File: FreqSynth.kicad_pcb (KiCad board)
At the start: 4 copper layers, 79 x 50 mm, 135 parts, among them IC1 ATMEGA32U2, P1 CPL-CON-BARREL-2.1MM, P2 RF1, P3 RF2P, P4 RF2N, P5 USB_MINI_B, P6 CONN_01X03, P7 REF_IN, P8 RESET, U1 MAX2870, U10 PE43711, U11 LMH2110, U2 TS5A3159, U3 TLV7113333DDSET, U4 AP65101, U5 TLV7113333DDSET, U6 RT9069-50GB, U7 SKY13322-375LF, U8 SKY13322-375LF, U9 TRF37A75, X1 25MHz ±5ppm 3.3V 33mA, X2 8MHz 18PF 50ppm

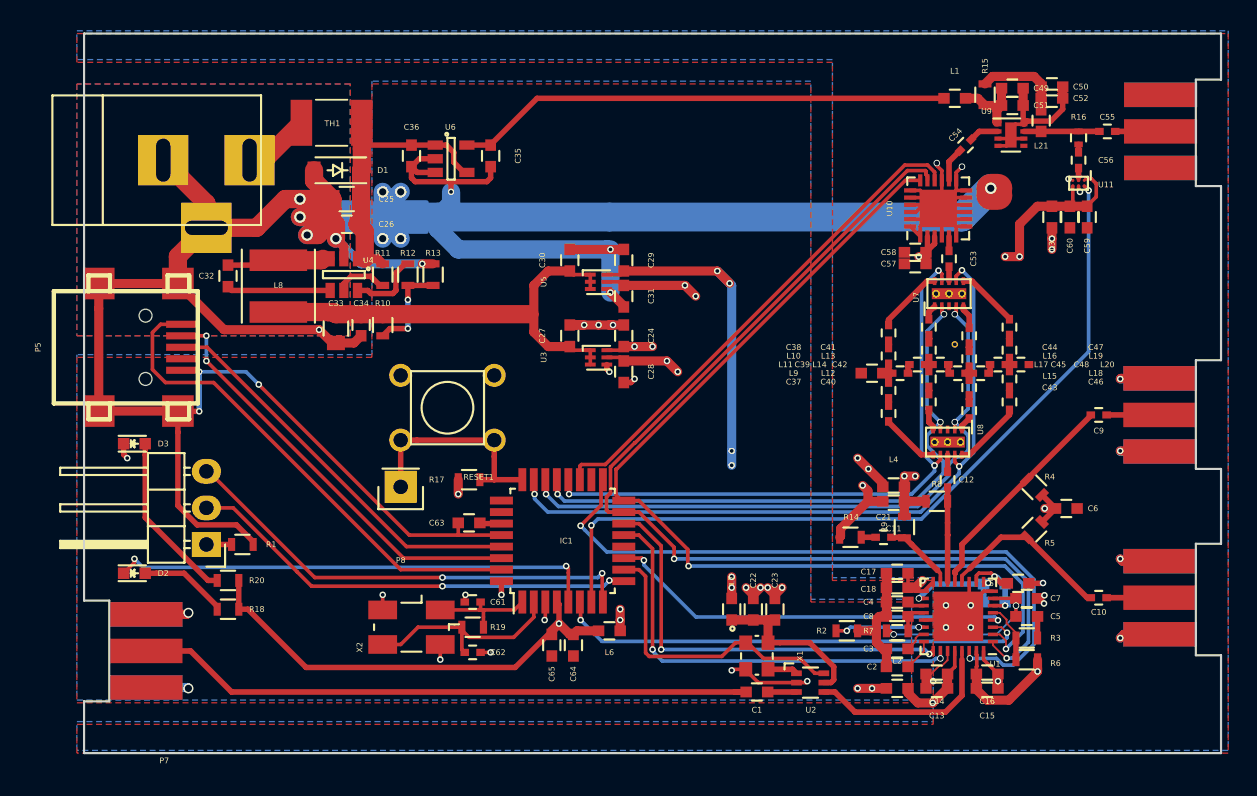
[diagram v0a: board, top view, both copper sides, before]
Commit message: Board layout done, no ERC or DRC:s left
Signed-off-by: Martin Berglund <LeastSignificantBit@users.noreply.github.com>
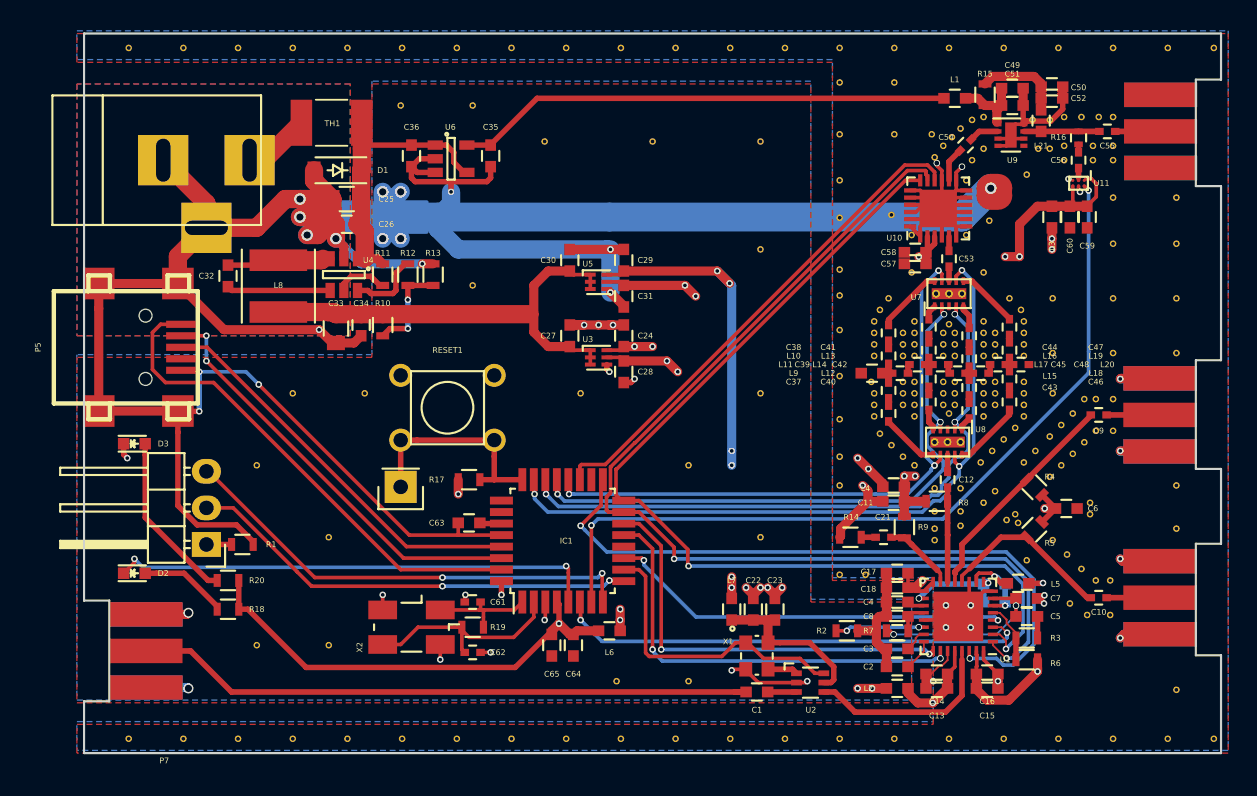
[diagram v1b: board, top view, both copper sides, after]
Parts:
- added ?: , FreqSynth:VIA, F.Cu at (142.5, 145.0)
- added ?: , FreqSynth:VIA, F.Cu at (127.5, 117.5)
- added ?: , FreqSynth:VIA, F.Cu at (126.4, 149.0)
- added ?: , FreqSynth:VIA, F.Cu at (107.4, 149.0)
- added ?: , FreqSynth:VIA, F.Cu at (111.2, 149.0)
- added ?: , FreqSynth:VIA, F.Cu at (115.0, 149.0)
- added ?: , FreqSynth:VIA, F.Cu at (103.6, 149.0)
- added ?: , FreqSynth:VIA, F.Cu at (175.8, 149.0)
- added ?: , FreqSynth:VIA, F.Cu at (172.0, 149.0)
- added ?: , FreqSynth:VIA, F.Cu at (179.0, 149.0)
- added ?: , FreqSynth:VIA, F.Cu at (149.2, 149.0)
- added ?: , FreqSynth:VIA, F.Cu at (153.0, 149.0)
- added ?: , FreqSynth:VIA, F.Cu at (117.5, 135.0)
- added ?: , FreqSynth:VIA, F.Cu at (156.8, 149.0)
- added ?: , FreqSynth:VIA, F.Cu at (160.6, 149.0)
- added ?: , FreqSynth:VIA, F.Cu at (168.2, 149.0)
- added ?: , FreqSynth:VIA, F.Cu at (164.4, 149.0)
- added ?: , FreqSynth:VIA, F.Cu at (115.0, 101.0)
- added ?: , FreqSynth:VIA, F.Cu at (111.2, 101.0)
- added ?: , FreqSynth:VIA, F.Cu at (126.4, 101.0)
- added ?: , FreqSynth:VIA, F.Cu at (103.6, 101.0)
- added ?: , FreqSynth:VIA, F.Cu at (107.4, 101.0)
- added ?: , FreqSynth:VIA, F.Cu at (122.6, 101.0)
- added ?: , FreqSynth:VIA, F.Cu at (112.5, 130.0)
- added ?: , FreqSynth:VIA, F.Cu at (118.8, 101.0)
- added ?: , FreqSynth:VIA, F.Cu at (130.2, 101.0)
- added ?: , FreqSynth:VIA, F.Cu at (137.8, 101.0)
- added ?: , FreqSynth:VIA, F.Cu at (134.0, 101.0)
- added ?: , FreqSynth:VIA, F.Cu at (145.4, 101.0)
- added ?: , FreqSynth:VIA, F.Cu at (149.2, 101.0)
- added ?: , FreqSynth:VIA, F.Cu at (141.6, 101.0)
- added ?: , FreqSynth:VIA, F.Cu at (179.0, 101.0)
- added ?: , FreqSynth:VIA, F.Cu at (175.8, 101.0)
- added ?: , FreqSynth:VIA, F.Cu at (164.4, 101.0)
- added ?: , FreqSynth:VIA, F.Cu at (120.0, 125.0)
- added ?: , FreqSynth:VIA, F.Cu at (160.6, 101.0)
- added ?: , FreqSynth:VIA, F.Cu at (172.0, 101.0)
- added ?: , FreqSynth:VIA, F.Cu at (168.2, 101.0)
- added ?: , FreqSynth:VIA, F.Cu at (156.8, 101.0)
- added ?: , FreqSynth:VIA, F.Cu at (153.0, 101.0)
- added ?: , FreqSynth:VIA, F.Cu at (153.0, 103.4)
- added ?: , FreqSynth:VIA, F.Cu at (153.0, 107.0)
- added ?: , FreqSynth:VIA, F.Cu at (156.6, 112.6)
- added ?: , FreqSynth:VIA, F.Cu at (153.0, 110.2)
- added ?: , FreqSynth:VIA, F.Cu at (153.0, 112.8)
- added ?: , FreqSynth:VIA, F.Cu at (135.0, 125.0)
- added ?: , FreqSynth:VIA, F.Cu at (153.0, 116.4)
- added ?: , FreqSynth:VIA, F.Cu at (153.0, 118.2)
- added ?: , FreqSynth:VIA, F.Cu at (153.0, 120.6)
- added ?: , FreqSynth:VIA, F.Cu at (153.0, 123.8)
- added ?: , FreqSynth:VIA, F.Cu at (153.0, 126.8)
- added ?: , FreqSynth:VIA, F.Cu at (153.0, 129.4)
- added ?: , FreqSynth:VIA, F.Cu at (153.0, 131.4)
- added ?: , FreqSynth:VIA, F.Cu at (153.0, 137.6)
- added ?: , FreqSynth:VIA, F.Cu at (154.8, 137.6)
- added ?: , FreqSynth:VIA, F.Cu at (159.6, 134.4)
- added ?: , FreqSynth:VIA, F.Cu at (142.5, 130.0)
- added ?: , FreqSynth:VIA, F.Cu at (163.0, 132.6)
- added ?: , FreqSynth:VIA, F.Cu at (159.6, 131.6)
- added ?: , FreqSynth:VIA, F.Cu at (159.6, 135.2)
- added ?: , FreqSynth:VIA, F.Cu at (159.6, 133.2)
- added ?: , FreqSynth:VIA, F.Cu at (161.4, 134.2)
- added ?: , FreqSynth:VIA, F.Cu at (161.4, 133.2)
- added ?: , FreqSynth:VIA, F.Cu at (161.4, 131.6)
- added ?: , FreqSynth:VIA, F.Cu at (162.8, 129.8)
- added ?: , FreqSynth:VIA, F.Cu at (163.6, 129.0)
- added ?: , FreqSynth:VIA, F.Cu at (165.2, 127.4)
- added ?: , FreqSynth:VIA, F.Cu at (147.5, 125.0)
- added ?: , FreqSynth:VIA, F.Cu at (164.4, 128.2)
- added ?: , FreqSynth:VIA, F.Cu at (165.8, 126.6)
- added ?: , FreqSynth:VIA, F.Cu at (165.8, 125.8)
- added ?: , FreqSynth:VIA, F.Cu at (165.8, 125.0)
- added ?: , FreqSynth:VIA, F.Cu at (165.8, 124.2)
- added ?: , FreqSynth:VIA, F.Cu at (165.8, 122.4)
- added ?: , FreqSynth:VIA, F.Cu at (165.8, 121.6)
- added ?: , FreqSynth:VIA, F.Cu at (165.8, 120.8)
- added ?: , FreqSynth:VIA, F.Cu at (165.8, 120.0)
- added ?: , FreqSynth:VIA, F.Cu at (165.6, 119.2)
- added ?: , FreqSynth:VIA, F.Cu at (132.5, 107.5)
- added ?: , FreqSynth:VIA, F.Cu at (164.8, 118.4)
- added ?: , FreqSynth:VIA, F.Cu at (163.0, 116.6)
- added ?: , FreqSynth:VIA, F.Cu at (158.0, 116.6)
- added ?: , FreqSynth:VIA, F.Cu at (156.4, 118.4)
- added ?: , FreqSynth:VIA, F.Cu at (155.8, 119.2)
- added ?: , FreqSynth:VIA, F.Cu at (155.4, 120.0)
- added ?: , FreqSynth:VIA, F.Cu at (155.4, 120.8)
- added ?: , FreqSynth:VIA, F.Cu at (155.4, 121.6)
- added ?: , FreqSynth:VIA, F.Cu at (155.4, 122.4)
- added ?: , FreqSynth:VIA, F.Cu at (155.2, 124.2)
- added ?: , FreqSynth:VIA, F.Cu at (140.0, 107.5)
- added ?: , FreqSynth:VIA, F.Cu at (155.4, 125.0)
- added ?: , FreqSynth:VIA, F.Cu at (155.4, 126.6)
- added ?: , FreqSynth:VIA, F.Cu at (155.4, 125.8)
- added ?: , FreqSynth:VIA, F.Cu at (155.8, 127.8)
- added ?: , FreqSynth:VIA, F.Cu at (156.6, 128.6)
- added ?: , FreqSynth:VIA, F.Cu at (157.4, 129.4)
- added ?: , FreqSynth:VIA, F.Cu at (158.2, 130.0)
- added ?: , FreqSynth:VIA, F.Cu at (158.2, 126.6)
- added ?: , FreqSynth:VIA, F.Cu at (158.2, 125.8)
- added ?: , FreqSynth:VIA, F.Cu at (157.4, 125.8)
- added ?: , FreqSynth:VIA, F.Cu at (147.5, 107.5)
- added ?: , FreqSynth:VIA, F.Cu at (158.2, 125.0)
- added ?: , FreqSynth:VIA, F.Cu at (157.4, 125.0)
- added ?: , FreqSynth:VIA, F.Cu at (157.4, 124.2)
- added ?: , FreqSynth:VIA, F.Cu at (163.0, 126.6)
- added ?: , FreqSynth:VIA, F.Cu at (163.8, 125.8)
- added ?: , FreqSynth:VIA, F.Cu at (163.0, 125.8)
- added ?: , FreqSynth:VIA, F.Cu at (163.0, 125.0)
- added ?: , FreqSynth:VIA, F.Cu at (163.8, 125.0)
- added ?: , FreqSynth:VIA, F.Cu at (163.8, 124.2)
- added ?: , FreqSynth:VIA, F.Cu at (163.0, 124.2)
- added ?: , FreqSynth:VIA, F.Cu at (137.5, 145.0)
- added ?: , FreqSynth:VIA, F.Cu at (161.8, 110.2)
- added ?: , FreqSynth:VIA, F.Cu at (160.6, 126.4)
- added ?: , FreqSynth:VIA, F.Cu at (160.2, 125.8)
- added ?: , FreqSynth:VIA, F.Cu at (161.0, 125.8)
- added ?: , FreqSynth:VIA, F.Cu at (161.0, 125.0)
- added ?: , FreqSynth:VIA, F.Cu at (160.2, 125.0)
- added ?: , FreqSynth:VIA, F.Cu at (160.2, 124.2)
- added ?: , FreqSynth:VIA, F.Cu at (161.0, 124.2)
- added ?: , FreqSynth:VIA, F.Cu at (163.8, 122.4)
- added ?: , FreqSynth:VIA, F.Cu at (163.0, 122.4)
- added ?: , FreqSynth:VIA, F.Cu at (163.0, 121.6)
- added ?: , FreqSynth:VIA, F.Cu at (158.0, 114.0)
- added ?: , FreqSynth:VIA, F.Cu at (163.8, 121.6)
- added ?: , FreqSynth:VIA, F.Cu at (163.8, 120.8)
- added ?: , FreqSynth:VIA, F.Cu at (163.0, 120.8)
- added ?: , FreqSynth:VIA, F.Cu at (163.0, 120.0)
- added ?: , FreqSynth:VIA, F.Cu at (158.2, 120.0)
- added ?: , FreqSynth:VIA, F.Cu at (158.2, 124.2)
- added ?: , FreqSynth:VIA, F.Cu at (158.2, 120.8)
- added ?: , FreqSynth:VIA, F.Cu at (157.4, 120.8)
- added ?: , FreqSynth:VIA, F.Cu at (157.4, 121.6)
- added ?: , FreqSynth:VIA, F.Cu at (158.2, 121.6)
- added ?: , FreqSynth:VIA, F.Cu at (161.8, 114.0)
- added ?: , FreqSynth:VIA, F.Cu at (158.2, 122.4)
- added ?: , FreqSynth:VIA, F.Cu at (157.4, 122.4)
- added ?: , FreqSynth:VIA, F.Cu at (160.6, 120.2)
- added ?: , FreqSynth:VIA, F.Cu at (161.0, 120.8)
- added ?: , FreqSynth:VIA, F.Cu at (160.2, 120.8)
- added ?: , FreqSynth:VIA, F.Cu at (160.2, 122.4)
- added ?: , FreqSynth:VIA, F.Cu at (160.2, 121.6)
- added ?: , FreqSynth:VIA, F.Cu at (161.0, 122.4)
- added ?: , FreqSynth:VIA, F.Cu at (166.0, 136.6)
- added ?: , FreqSynth:VIA, F.Cu at (171.8, 140.4)
- added ?: , FreqSynth:VIA, F.Cu at (170.2, 140.4)
- added ?: , FreqSynth:VIA, F.Cu at (169.0, 139.6)
- added ?: , FreqSynth:VIA, F.Cu at (163.8, 131.8)
- added ?: , FreqSynth:VIA, F.Cu at (165.8, 129.8)
- added ?: , FreqSynth:VIA, F.Cu at (166.6, 129.0)
- added ?: , FreqSynth:VIA, F.Cu at (122.5, 105.0)
- added ?: , FreqSynth:VIA, F.Cu at (167.6, 128.0)
- added ?: , FreqSynth:VIA, F.Cu at (168.4, 127.2)
- added ?: , FreqSynth:VIA, F.Cu at (169.2, 126.4)
- added ?: , FreqSynth:VIA, F.Cu at (170.0, 125.4)
- added ?: , FreqSynth:VIA, F.Cu at (170.8, 125.4)
- added ?: , FreqSynth:VIA, F.Cu at (172.0, 125.4)
- added ?: , FreqSynth:VIA, F.Cu at (172.0, 127.6)
- added ?: , FreqSynth:VIA, F.Cu at (170.8, 127.6)
- added ?: , FreqSynth:VIA, F.Cu at (170.0, 128.4)
- added ?: , FreqSynth:VIA, F.Cu at (169.2, 129.2)
- added ?: , FreqSynth:VIA, F.Cu at (127.5, 105.0)
- added ?: , FreqSynth:VIA, F.Cu at (168.4, 130.0)
- added ?: , FreqSynth:VIA, F.Cu at (167.6, 130.8)
- added ?: , FreqSynth:VIA, F.Cu at (171.8, 138.0)
- added ?: , FreqSynth:VIA, F.Cu at (170.8, 138.0)
- added ?: , FreqSynth:VIA, F.Cu at (169.8, 137.2)
- added ?: , FreqSynth:VIA, F.Cu at (168.8, 136.2)
- added ?: , FreqSynth:VIA, F.Cu at (167.8, 135.2)
- added ?: , FreqSynth:VIA, F.Cu at (165.4, 134.0)
- added ?: , FreqSynth:VIA, F.Cu at (165.2, 133.4)
- added ?: , FreqSynth:VIA, F.Cu at (164.6, 133.8)
- added ?: , FreqSynth:VIA, F.Cu at (112.5, 142.5)
- added ?: , FreqSynth:VIA, F.Cu at (170.4, 132.6)
- added ?: , FreqSynth:VIA, F.Cu at (170.4, 133.4)
- added ?: , FreqSynth:VIA, F.Cu at (167.8, 125.0)
- added ?: , FreqSynth:VIA, F.Cu at (167.8, 122.2)
- added ?: , FreqSynth:VIA, F.Cu at (167.8, 118.4)
- added ?: , FreqSynth:VIA, F.Cu at (163.4, 113.0)
- added ?: , FreqSynth:VIA, F.Cu at (166.0, 109.8)
- added ?: , FreqSynth:VIA, F.Cu at (172.0, 108.8)
- added ?: , FreqSynth:VIA, F.Cu at (170.6, 108.8)
- added ?: , FreqSynth:VIA, F.Cu at (168.6, 108.8)
- added ?: , FreqSynth:VIA, F.Cu at (115.0, 125.0)
- added ?: , FreqSynth:VIA, F.Cu at (166.8, 108.0)
- added ?: , FreqSynth:VIA, F.Cu at (167.6, 108.0)
- added ?: , FreqSynth:VIA, F.Cu at (168.6, 107.8)
- added ?: , FreqSynth:VIA, F.Cu at (170.6, 107.8)
- added ?: , FreqSynth:VIA, F.Cu at (172.0, 107.8)
- added ?: , FreqSynth:VIA, F.Cu at (172.0, 105.8)
- added ?: , FreqSynth:VIA, F.Cu at (171.0, 105.8)
- added ?: , FreqSynth:VIA, F.Cu at (169.8, 105.8)
- added ?: , FreqSynth:VIA, F.Cu at (168.6, 105.8)
- added ?: , FreqSynth:VIA, F.Cu at (166.4, 106.0)
- added ?: , FreqSynth:VIA, F.Cu at (147.5, 135.0)
- added ?: , FreqSynth:VIA, F.Cu at (167.6, 106.0)
- added ?: , FreqSynth:VIA, F.Cu at (159.6, 108.6)
- added ?: , FreqSynth:VIA, F.Cu at (160.2, 107.8)
- added ?: , FreqSynth:VIA, F.Cu at (160.8, 107.2)
- added ?: , FreqSynth:VIA, F.Cu at (161.4, 106.6)
- added ?: , FreqSynth:VIA, F.Cu at (162.2, 106.0)
- added ?: , FreqSynth:VIA, F.Cu at (163.0, 105.8)
- added ?: , FreqSynth:VIA, F.Cu at (163.0, 108.0)
- added ?: , FreqSynth:VIA, F.Cu at (162.2, 108.8)
- added ?: , FreqSynth:VIA, F.Cu at (172.0, 122.2)
- added ?: , FreqSynth:VIA, F.Cu at (117.5, 142.5)
- added ?: , FreqSynth:VIA, F.Cu at (172.0, 118.4)
- added ?: , FreqSynth:VIA, F.Cu at (172.0, 114.6)
- added ?: , FreqSynth:VIA, F.Cu at (172.0, 111.4)
- added ?: , FreqSynth:VIA, F.Cu at (156.8, 103.4)
- added ?: , FreqSynth:VIA, F.Cu at (156.8, 107.0)
- added ?: , FreqSynth:VIA, F.Cu at (159.4, 107.0)
- added ?: , FreqSynth:VIA, F.Cu at (176.4, 134.4)
- added ?: , FreqSynth:VIA, F.Cu at (176.4, 145.6)
- added ?: , FreqSynth:VIA, F.Cu at (176.4, 131.4)
- added ?: , FreqSynth:VIA, F.Cu at (176.4, 118.4)
- added ?: , FreqSynth:VIA, F.Cu at (147.5, 115.0)
- added ?: , FreqSynth:VIA, F.Cu at (176.4, 111.4)
- added ?: , FreqSynth:VIA, F.Cu at (176.4, 114.6)
- added ?: , FreqSynth:VIA, F.Cu at (176.4, 122.2)
- added ?: , FreqSynth:VIA, F.Cu at (145.4, 149.0)
- added ?: , FreqSynth:VIA, F.Cu at (130.2, 149.0)
- added ?: , FreqSynth:VIA, F.Cu at (134.0, 149.0)
- added ?: , FreqSynth:VIA, F.Cu at (141.6, 149.0)
- added ?: , FreqSynth:VIA, F.Cu at (137.8, 149.0)
- added ?: , FreqSynth:VIA, F.Cu at (118.8, 149.0)
- added ?: , FreqSynth:VIA, F.Cu at (122.6, 149.0)
- added G***: LOGO, FreqSynth:Logo_silk_polarity_center_5x1.4mm, B.Cu at (103.0, 109.0)
- added G***: LOGO, FreqSynth:Logo_silk_WEEE_3.4x5mm, B.Cu at (121.8, 144.8)
- added G***: LOGO, FreqSynth:Logo_silk_OSHW_6x6mm, B.Cu at (128.0, 144.2)
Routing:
- net /MCU/ADC1: track 56.5 -> 57.4 mm
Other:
- net class 50Ohm removed
- rule pad_to_mask_clearance: 0 -> 0.05
- board text added: "6.5 - 16V >0.8 A"
- board text added: "Frequency Synthesizer V 1.0 Martin Berglund 2016"
- board text added: "REF IN"
- board text added: "RF 1"
- board text added: "RF 2 +"
- board text added: "RF 2 -"
- board text added: "Tx Rx GND"

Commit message: Major rework
Removed star ground.
Switched MCU.
Smaller board outline - Ripped up almost the entire ratsnest.
Eliminated one crystal.
No more USB
New debug header
Eliminated reset switch
Only single ended RF2
And much more

Signed-off-by: Martin Berglund <LeastSignificantBit@users.noreply.github.com>
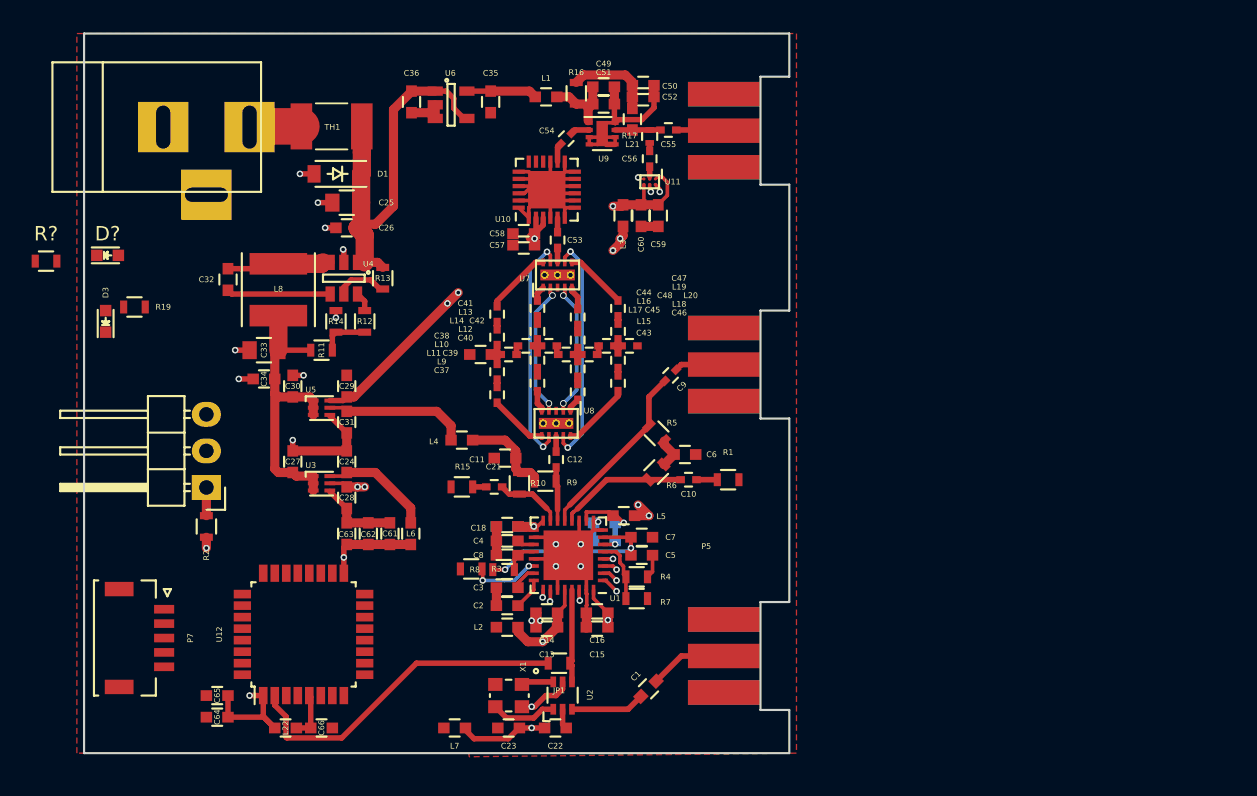
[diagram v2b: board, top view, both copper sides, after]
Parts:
- removed ? (x228): , FreqSynth:VIA
- removed the C62 at (127.5, 143.0)
- removed the C63 at (127.2, 134.0)
- removed the D3 at (104.0, 128.5)
- removed G***: LOGO, FreqSynth:Logo_silk_polarity_center_5x1.4mm
- removed G***: LOGO, FreqSynth:Logo_silk_WEEE_3.4x5mm
- removed G***: LOGO, FreqSynth:Logo_silk_OSHW_6x6mm
- removed IC1: ATMEGA32U2, Housings_QFP:TQFP-32_7x7mm_Pitch0.8mm
- removed the P4 at (175.2, 126.5)
- removed the P5 at (103.4, 121.8)
- removed P8: RESET, Pin_Headers:Pin_Header_Straight_1x01
- removed the R17 at (127.2, 131.0)
- removed the R19 at (127.5, 141.2)
- removed R20: 33R, Resistors_SMD:R_0603
- removed RESET1: B3F-1000, FreqSynth:SW_B3F-1000
- removed SG1: StarGND, FreqSynth:NetTie-II_Connected_SMD
- removed X2: 8MHz 18PF 50ppm, Crystals:Crystal_SMD_5032_4Pads
- added C64: 10nF, Capacitors_SMD:C_0603, F.Cu at (109.8, 147.5)
- added C65: 100pF, Capacitors_SMD:C_0603, F.Cu at (109.8, 146.0)
- added C66: 10nF, Capacitors_SMD:C_0603, F.Cu at (117.0, 148.2)
- added D?: GREEN, LEDs:LED_0603, F.Cu at (102.1, 115.4)
- added JP1: Jumper_NC_Small, Resistors_SMD:R_0603, F.Cu at (133.5, 143.8)
- added L22: Ferrite, FreqSynth:L_0603, F.Cu at (114.5, 148.2)
- added P7: SWD, Connectors_JST:JST_SHL_SM05B-SHLS-TF_05x1.00mm_Angled, F.Cu at (104.5, 142.0)
- added R1: 49.9R, Resistors_SMD:R_0603, F.Cu at (145.2, 131.0)
- added R?: 33R, Resistors_SMD:R_0603, F.Cu at (97.9, 115.8)
- added U12: STM32F030K6T6, Housings_QFP:LQFP-32_7x7mm_Pitch0.8mm, F.Cu at (115.8, 141.8)
- C17: moved to B.Cu
- C61: value 22p -> 1µF; footprint Capacitors_SMD:C_0402 -> Capacitors_SMD:C_0603
- D3: renamed from D2; value CPL-LED-0603-YELLOW -> YELLOW
- P3: value RF2P -> RF2
- moved P5 40.2 mm to (145.0, 143.2), turned to 0 degrees
- moved P3 34.3 mm to (145.0, 123.0)
- moved C55 30.5 mm to (141.1, 106.7)
- moved P2 30.3 mm to (145.0, 106.8)
- moved L4 30.2 mm to (126.8, 128.2)
- moved C9 29.9 mm to (141.2, 123.8), turned to 225 degrees
- moved C60 29.8 mm to (139.2, 112.7)
- moved L3 29.8 mm to (137.9, 112.7)
- moved C56 29.8 mm to (139.8, 108.7)
- moved C59 29.8 mm to (140.4, 112.7)
- moved R17 29.8 mm to (139.8, 107.2)
- moved U11 29.8 mm to (139.8, 110.3)
- moved C10 29.7 mm to (142.5, 131.0)
- moved C49 28.4 mm to (136.6, 103.7)
- moved C50 28.4 mm to (139.3, 103.6)
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- renumbered C64 to C62, C65 to C63, P6 to P4, P7 to P5, R9 to R10, R10 to R11, R11 to R12, R12 to R13, R13 to R14, R14 to R15, R15 to R16, R16 to R17, R18 to R19, R1 to R2, R2 to R3, R3 to R4, R4 to R5, R5 to R6, R6 to R7, R7 to R8, R8 to R9
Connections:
- C13 pad 2: GNDD -> Earth
- C14 pad 2: GNDD -> Earth
- C15 pad 2: GNDD -> Earth
- C16 pad 2: GNDD -> Earth
- C19 pad 2: GNDD -> Earth
- C20 pad 2: GNDD -> Earth
- C22 pad 2: GNDD -> Earth
- C23 pad 2: GNDD -> Earth
- C24 pad 1: GNDD -> Earth
- C25 pad 2: GNDPWR -> Earth
- C26 pad 2: GNDPWR -> Earth
- C27 pad 2: GNDD -> Earth
- C33 pad 2: GNDPWR -> Earth
- C34 pad 2: GNDPWR -> Earth
- C61 pad 1: GNDD -> /MCU/VCC_D
- C61 pad 2: Net-(C61-Pad2) -> Earth
- C62 pad 2: GNDD -> Earth
- C63 pad 2: GNDD -> Earth
- D1 pad 2: GNDPWR -> Earth
- P1 pad 2: GNDPWR -> Earth
- P1 pad 3: GNDPWR -> Earth
- P3 pad 1: /PLL/RF_BALANCED+ -> /PLL/RF_BALANCED-
- P5 pad 2: GNDD -> Earth
- R14 pad 1: GNDPWR -> Earth
- R2 pad 2: GNDPWR -> Earth
- R7 pad 1: GNDD -> Earth
- U1 pad 18: GNDD -> Earth
- U1 pad 27: GNDD -> Earth
- U1 pad 31: GNDD -> Earth
- U1 pad 9: GNDD -> Earth
- U2 pad 2: GNDD -> Earth
- U3 pad 4: GNDD -> Earth
- U4 pad 2: GNDPWR -> Earth
- U9 pad 5: Net-(U9-Pad5) -> Earth
- X1 pad 2: GNDD -> Earth
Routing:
- net GNDPWR: track 127.0 -> 0.00 mm, vias 9 -> 0
- net Earth: track 170.9 -> 88.9 mm, vias 20 -> 19
- net GNDD: track 73.4 -> 0.00 mm, vias 26 -> 0
- net /SCK: track 73.8 -> 1.26 mm, vias 2 -> 1
- net /MOSI: track 69.6 -> 1.16 mm, vias 2 -> 1
- net /MCU/ADC1: track 57.4 -> 0.62 mm, vias 2 -> 1
- net /Power/VCC_D: track 60.9 -> 7.78 mm, vias 6 -> 0
- net /MISO: track 47.2 -> 0.77 mm, vias 2 -> 1
- net Net-(C1-Pad2): track 43.7 -> 5.47 mm
- net /FILT3: track 44.9 -> 9.37 mm, vias 3 -> 2
- net /Amplifier/ATTEN_CS: track 35.0 -> 0.00 mm
- net /MCU/V_USB: track 34.9 -> 0.00 mm
- net Net-(D3-Pad1): track 34.2 -> 0.00 mm, vias 2 -> 0
- net /FILT2: track 49.5 -> 16.3 mm, vias 3 -> 2
- net /FILT4: track 42.7 -> 9.50 mm, vias 3 -> 2
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- removed copper zone on B.Cu, net Earth
- removed copper zone on In2.Cu, net Earth
- removed copper zone on B.Cu, net GNDD
- removed copper zone on F.Cu, net GNDD
- removed copper zone on In1.Cu, net GNDD
- removed copper zone on In2.Cu, net GNDD
- removed copper zone on B.Cu, net GNDPWR
- removed copper zone on F.Cu, net GNDPWR
- removed copper zone on In1.Cu, net GNDPWR
- removed copper zone on In2.Cu, net GNDPWR
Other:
- board size 79 x 50 mm -> 49 x 50 mm
- board text added: "RF 2"
- board text removed: "RF 2 +"
- board text removed: "RF 2 -"
